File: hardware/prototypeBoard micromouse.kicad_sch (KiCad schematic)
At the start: 10 parts, among them J1 Conn_01x02_Pin

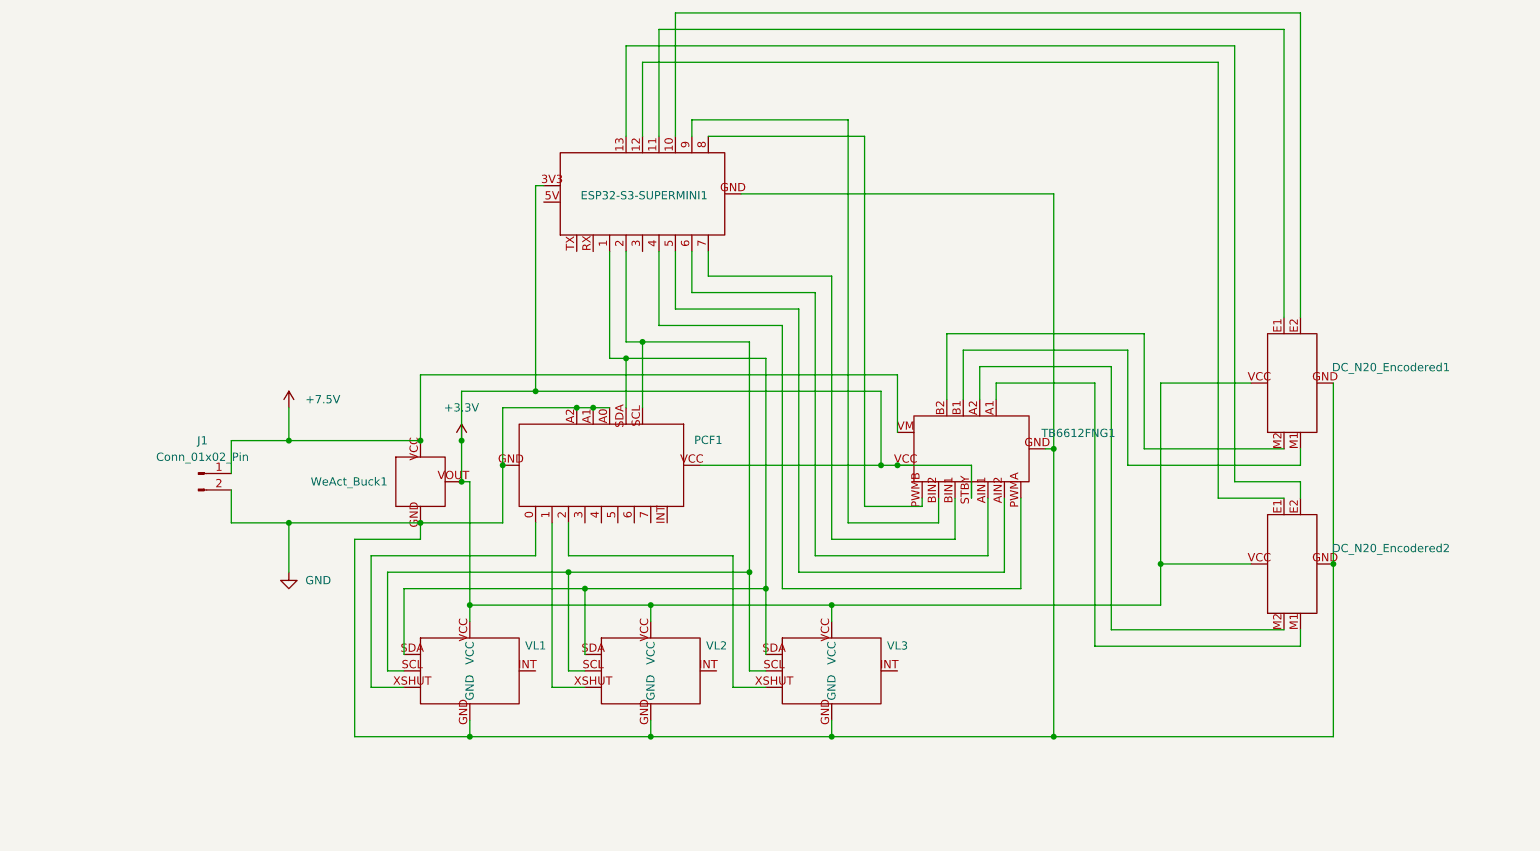
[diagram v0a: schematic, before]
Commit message: add switch + capacitors
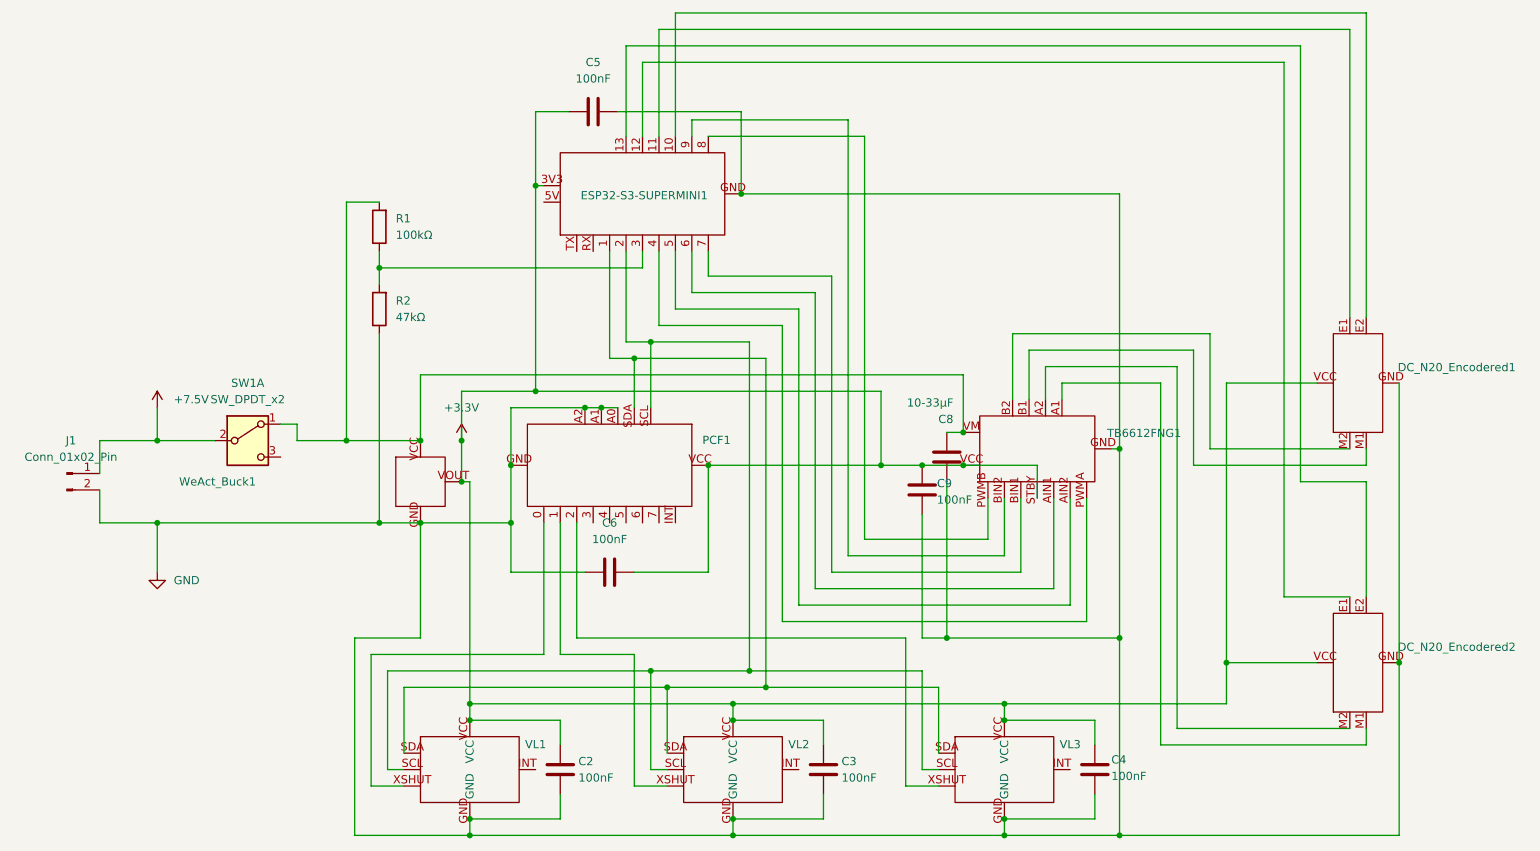
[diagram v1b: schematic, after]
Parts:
- added C2, C3, C4, C5, C6, C9: 100nF, symbol Device:C
- added C8: 10-33µF, symbol Device:C
- added R1: 100kΩ, symbol Device:R
- added R2: 47kΩ, symbol Device:R
- added SW1: SW_DPDT_x2, symbol Switch:SW_DPDT_x2
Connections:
- net +3.3V: now also C2.2, C3.2, C4.2, C5.2, C6.2, C9.1
- net +7.5V: now also SW1.2 (B); no longer TB6612FNG1.VM, WeAct_Buck1.VCC
- net GND: now also C2.1, C3.1, C4.1, C5.1, C6.1, C8.1, C9.2, R2.1
- net at ESP32-S3-SUPERMINI1.3: now also R1.1, R2.2
- new net: C8.2, R1.2, SW1.1 (A), TB6612FNG1.VM, WeAct_Buck1.VCC
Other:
- moved on the sheet: DC_N20_Encodered1, DC_N20_Encodered2, J1, PCF1, TB6612FNG1, VL1, VL2, VL3
